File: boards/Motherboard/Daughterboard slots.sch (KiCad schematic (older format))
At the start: 5 parts, among them P701 SLOT-A, P702 SLOT-B, P703 SLOT-C, P704 SLOT-D, P705 SLOT-E

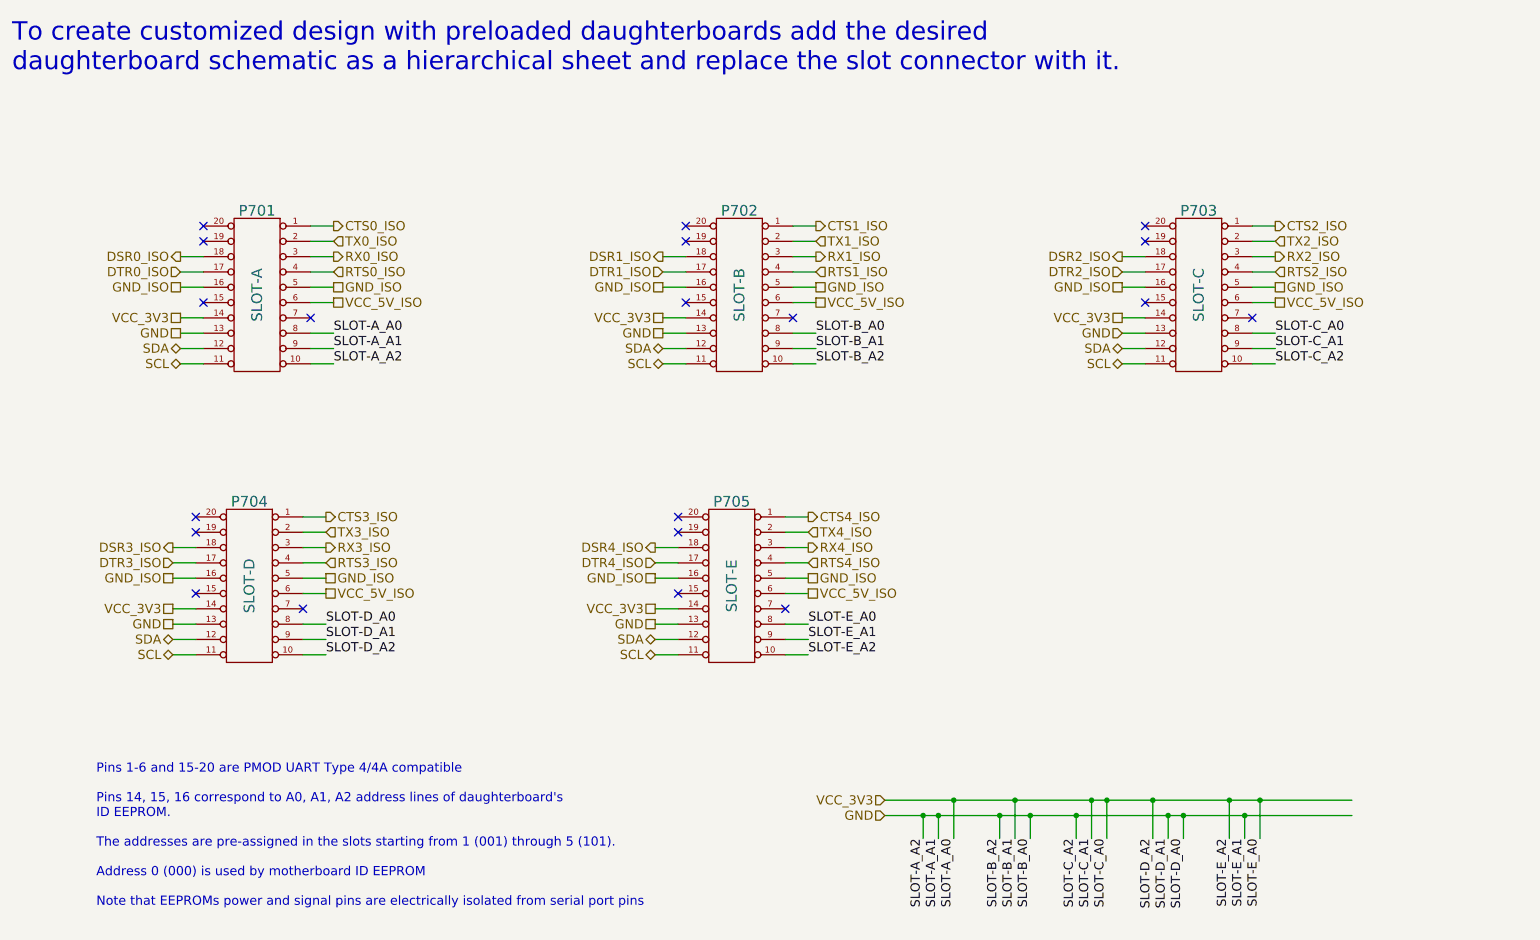
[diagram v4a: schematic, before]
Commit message: Rearranged EEPROM pins in dboard slot pinout to be compatible with PMOD I2C interface
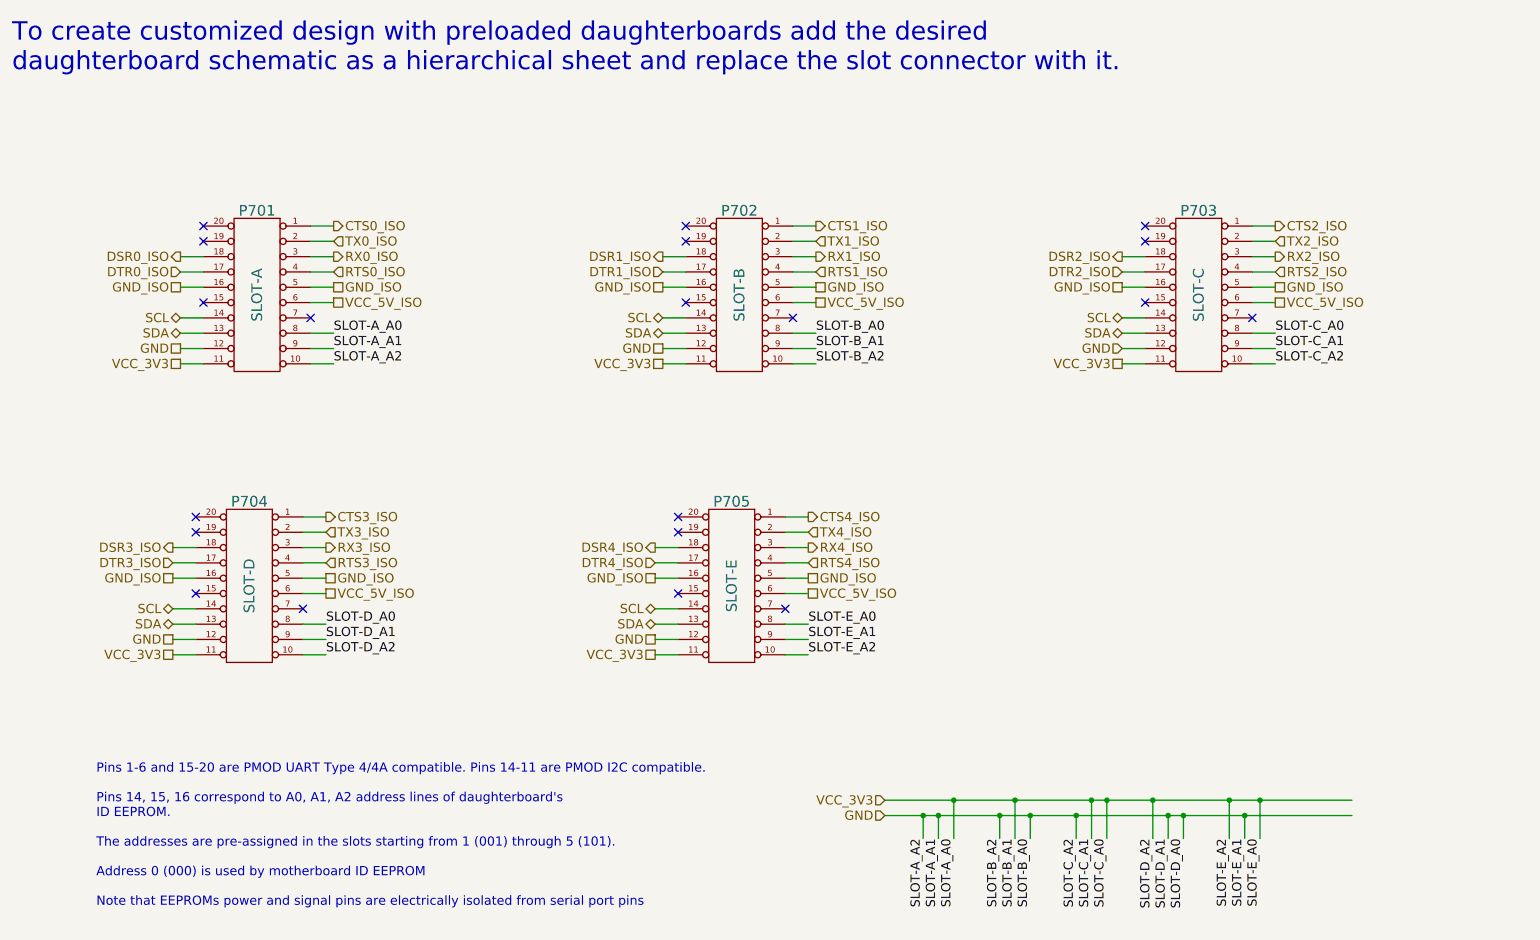
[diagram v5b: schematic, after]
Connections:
- net GND: now also P701.12 (P12), P702.12 (P12), P703.12 (P12), P704.12 (P12), P705.12 (P12); no longer P701.13 (P13), P702.13 (P13), P703.13 (P13), P704.13 (P13), P705.13 (P13)
- net SCL: now also P701.14 (P14), P702.14 (P14), P703.14 (P14), P704.14 (P14), P705.14 (P14); no longer P701.11 (P11), P702.11 (P11), P703.11 (P11), P704.11 (P11), P705.11 (P11)
- net SDA: now also P701.13 (P13), P702.13 (P13), P703.13 (P13), P704.13 (P13), P705.13 (P13); no longer P701.12 (P12), P702.12 (P12), P703.12 (P12), P704.12 (P12), P705.12 (P12)
- net VCC_3V3: now also P701.11 (P11), P702.11 (P11), P703.11 (P11), P704.11 (P11), P705.11 (P11); no longer P701.14 (P14), P702.14 (P14), P703.14 (P14), P704.14 (P14), P705.14 (P14)
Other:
- note added: "Pins 1-6 and 15-20 are PMOD UART Type 4/4A compatible. Pins 14-11 are PMOD I2C compatible.\n\nPins 14, 15, 16 correspond to A0, A1, A2 address lines of daughterboard's \nID EEPROM. \n\nThe addresses are pre-assigned in the slots starting from 1 (001) through 5 (101).\n\nAddress 0 (000) is used by motherboard ID EEPROM\n\nNote that EEPROMs power and signal pins are electrically isolated from seria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"
- note removed: "Pins 1-6 and 15-20 are PMOD UART Type 4/4A compatible\n\nPins 14, 15, 16 correspond to A0, A1, A2 address lines of daughterboard's \nID EEPROM. \n\nThe addresses are pre-assigned in the slots starting from 1 (001) through 5 (101).\n\nAddress 0 (000) is used by motherboard ID EEPROM\n\nNote that EEPROMs power and signal pins are electrically isolated from serial port pins"
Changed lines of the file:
@@
 Sheet 5 7
 Title "Daughterboard interface"
-Date "1 jul 2014"
+Date "2 jul 2014"
 Rev ""
 Comp "TimVideos"
@@
 Text HLabel 3100 2550 2    60   UnSpc ~ 0
 GND_ISO
-Text HLabel 2100 2950 0    60   BiDi ~ 0
+Text HLabel 2100 2850 0    60   BiDi ~ 0
 SDA
 Text Notes 1000 1150 0    120  ~ 0
 To create customized design with preloaded daughterboards add the desired \ndaughterboard schematic as a hierarchical sheet and replace the slot connector with it.
-Text HLabel 2100 3050 0    60   BiDi ~ 0
+Text HLabel 2100 2750 0    60   BiDi ~ 0
 SCL
-Text HLabel 2100 2750 0    60   UnSpc ~ 0
-VCC_3V3
-Text HLabel 2100 2850 0    60   UnSpc ~ 0
+Text HLabel 2100 3050 0    60   UnSpc ~ 0
+VCC_3V3
+Text HLabel 2100 2950 0    60   UnSpc ~ 0
 GND
 Text Notes 1550 6600 0    60   ~ 0
-Pins 1-6 and 15-20 are PMOD UART Type 4/4A compatible\n\nPins 14, 15, 16 correspond to A0, A1, A2 address lines of daughterboard's \nID EEPROM. \n\nThe addresses are pre-assigned in the slots starting from 1 (001) through 5 (101).\n\nAddress 0 (000) is used by motherboard ID EEPROM\n\nNote that EEPROMs power and signal pins are electrically isolated from serial port pins
+Pins 1-6 and 15-20 are PMOD UART Type 4/4A compatible. Pins 14-11 are PMOD I2C compatible.\n\nPins 14, 15, 16 correspond to A0, A1, A2 address lines of daughterboard's \nID EEPROM. \n\nThe addresses are pre-assigned in the slots starting from 1 (001) through 5 (101).\n\nAddress 0 (000) is used by motherboard ID EEPROM\n\nNote that EEPROMs power and signal pins are electrically isolated from serial port pins
 Text Label 3100 2850 0    60   ~ 0
 SLOT-A_A0
@@
 GND
 NoConn ~ 2250 2650
-Text HLabel 5250 2950 0    60   BiDi ~ 0
+Text HLabel 5250 2850 0    60   BiDi ~ 0
 SDA
-Text HLabel 5250 3050 0    60   BiDi ~ 0
+Text HLabel 5250 2750 0    60   BiDi ~ 0
 SCL
-Text HLabel 5250 2850 0    60   UnSpc ~ 0
+Text HLabel 5250 2950 0    60   UnSpc ~ 0
 GND
 Text Label 6250 2850 0    60   ~ 0
@@
 Text Label 6250 3050 0    60   ~ 0
 SLOT-B_A2
-Text HLabel 8250 2950 0    60   BiDi ~ 0
+Text HLabel 8250 2850 0    60   BiDi ~ 0
 SDA
-Text HLabel 8250 3050 0    60   BiDi ~ 0
+Text HLabel 8250 2750 0    60   BiDi ~ 0
 SCL
-Text HLabel 8250 2850 0    60   Input ~ 0
+Text HLabel 8250 2950 0    60   Input ~ 0
 GND
 Text Label 9250 2850 0    60   ~ 0
@@
 	-1   0    0    -1
 $EndComp
-Text HLabel 2050 4850 0    60   BiDi ~ 0
+Text HLabel 2050 4750 0    60   BiDi ~ 0
 SDA
-Text HLabel 2050 4950 0    60   BiDi ~ 0
+Text HLabel 2050 4650 0    60   BiDi ~ 0
 SCL
-Text HLabel 2050 4750 0    60   UnSpc ~ 0
+Text HLabel 2050 4850 0    60   UnSpc ~ 0
 GND
 Text Label 3050 4750 0    60   ~ 0
@@
 	-1   0    0    -1
 $EndComp
-Text HLabel 5200 4850 0    60   BiDi ~ 0
+Text HLabel 5200 4750 0    60   BiDi ~ 0
 SDA
-Text HLabel 5200 4950 0    60   BiDi ~ 0
+Text HLabel 5200 4650 0    60   BiDi ~ 0
 SCL
-Text HLabel 5200 4750 0    60   UnSpc ~ 0
+Text HLabel 5200 4850 0    60   UnSpc ~ 0
 GND
 Text Label 6200 4750 0    60   ~ 0
@@
 	3100 2550 2950 2550
 Wire Wire Line
+	2100 2850 2250 2850
+Wire Wire Line
+	2100 2750 2250 2750
+Wire Wire Line
 	2100 2950 2250 2950
 Wire Wire Line
 	2100 3050 2250 3050
 Wire Wire Line
-	2100 2850 2250 2850
-Wire Wire Line
-	2100 2750 2250 2750
-Wire Wire Line
 	3100 2850 2950 2850
 Wire Wire Line
@@
 	6700 6000 9750 6000
 Wire Wire Line
+	5250 2850 5400 2850
+Wire Wire Line
+	5250 2750 5400 2750
+Wire Wire Line
 	5250 2950 5400 2950
 Wire Wire Line
-	5250 3050 5400 3050
-Wire Wire Line
-	5250 2850 5400 2850
-Wire Wire Line
 	6250 2850 6100 2850
 Wire Wire Line
@@
 	6250 3050 6100 3050
 Wire Wire Line
+	8250 2850 8400 2850
+Wire Wire Line
+	8250 2750 8400 2750
+Wire Wire Line
 	8250 2950 8400 2950
 Wire Wire Line
-	8250 3050 8400 3050
-Wire Wire Line
-	8250 2850 8400 2850
-Wire Wire Line
 	9250 2850 9100 2850
 Wire Wire Line
@@
 	9250 3050 9100 3050
 Wire Wire Line
+	2050 4750 2200 4750
+Wire Wire Line
+	2050 4650 2200 4650
+Wire Wire Line
 	2050 4850 2200 4850
 Wire Wire Line
-	2050 4950 2200 4950
-Wire Wire Line
-	2050 4750 2200 4750
-Wire Wire Line
 	3050 4750 2900 4750
 Wire Wire Line
@@
 	3050 4950 2900 4950
 Wire Wire Line
+	5200 4750 5350 4750
+Wire Wire Line
+	5200 4650 5350 4650
+Wire Wire Line
 	5200 4850 5350 4850
-Wire Wire Line
-	5200 4950 5350 4950
-Wire Wire Line
-	5200 4750 5350 4750
 Wire Wire Line
 	6200 4750 6050 4750
@@
 Wire Wire Line
 	6100 2450 6250 2450
-Text HLabel 5250 2750 0    60   UnSpc ~ 0
-VCC_3V3
-Wire Wire Line
-	5250 2750 5400 2750
+Text HLabel 5250 3050 0    60   UnSpc ~ 0
+VCC_3V3
+Wire Wire Line
+	5250 3050 5400 3050
 NoConn ~ 6100 2750
 Text HLabel 9250 2150 2    60   Output ~ 0
@@
 Wire Wire Line
 	8250 2550 8400 2550
-Text HLabel 8250 2750 0    60   UnSpc ~ 0
-VCC_3V3
-Wire Wire Line
-	8250 2750 8400 2750
+Text HLabel 8250 3050 0    60   UnSpc ~ 0
+VCC_3V3
+Wire Wire Line
+	8250 3050 8400 3050
 NoConn ~ 8400 2650
 NoConn ~ 8400 2250
@@
 NoConn ~ 2200 4550
 NoConn ~ 2900 4650
-Text HLabel 2050 4650 0    60   UnSpc ~ 0
-VCC_3V3
-Wire Wire Line
-	2050 4650 2200 4650
+Text HLabel 2050 4950 0    60   UnSpc ~ 0
+VCC_3V3
+Wire Wire Line
+	2050 4950 2200 4950
 NoConn ~ 6050 4650
 NoConn ~ 5350 4550
@@
 Wire Wire Line
 	5200 4450 5350 4450
-Text HLabel 5200 4650 0    60   UnSpc ~ 0
-VCC_3V3
-Wire Wire Line
-	5200 4650 5350 4650
+Text HLabel 5200 4950 0    60   UnSpc ~ 0
+VCC_3V3
+Wire Wire Line
+	5200 4950 5350 4950
 $EndSCHEMATC

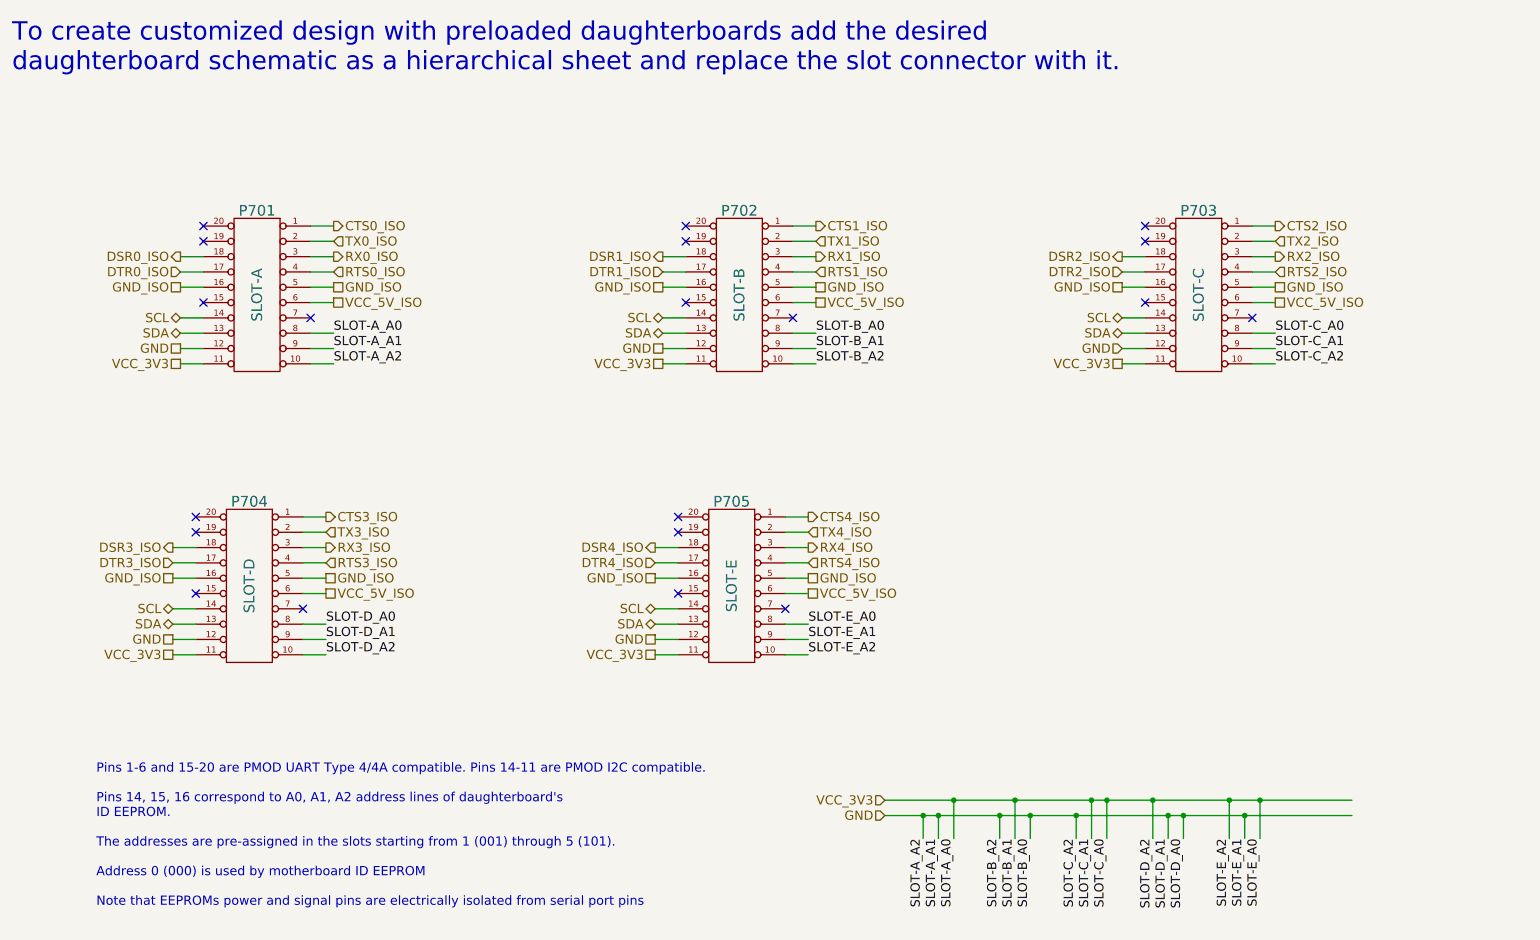
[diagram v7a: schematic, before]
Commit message: Updated motherboard schematic to use new dboard_slot component
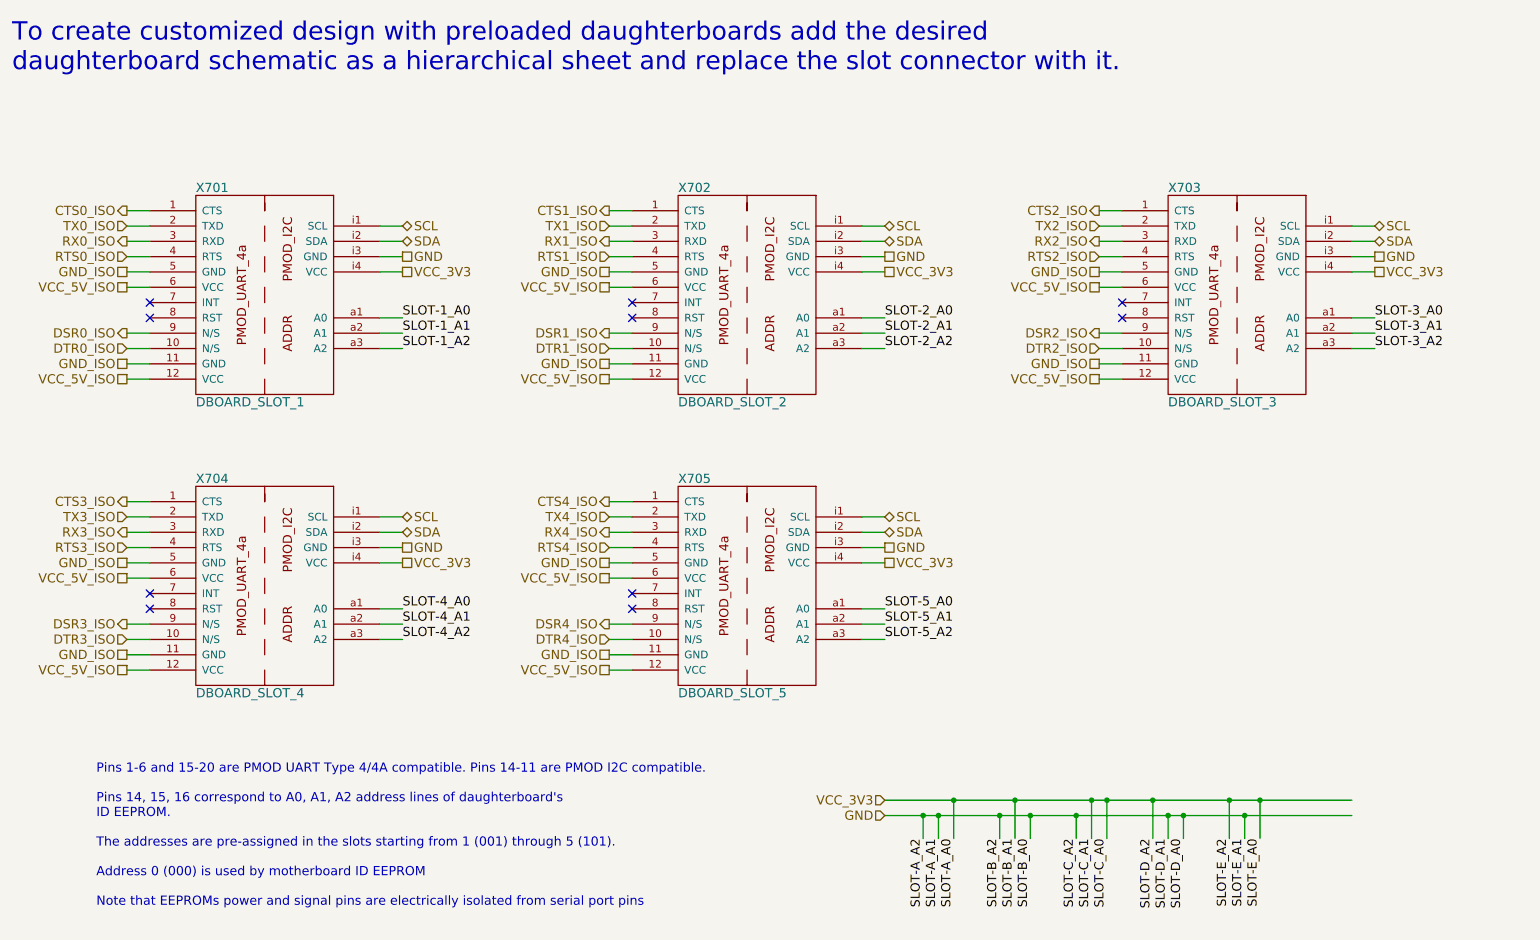
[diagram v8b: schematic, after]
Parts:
- removed P701: SLOT-A, symbol DIL20
- removed P702: SLOT-B, symbol DIL20
- removed P703: SLOT-C, symbol DIL20
- removed P704: SLOT-D, symbol DIL20
- removed P705: SLOT-E, symbol DIL20
- added X701: DBOARD_SLOT_1, ~, symbol DBOARD_SLOT
- added X702: DBOARD_SLOT_2, ~, symbol DBOARD_SLOT
- added X703: DBOARD_SLOT_3, ~, symbol DBOARD_SLOT
- added X704: DBOARD_SLOT_4, ~, symbol DBOARD_SLOT
- added X705: DBOARD_SLOT_5, ~, symbol DBOARD_SLOT
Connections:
- net CTS0_ISO: now also X701.1 (CTS)
- net CTS1_ISO: now also X702.1 (CTS)
- net CTS2_ISO: now also X703.1 (CTS)
- net CTS3_ISO: now also X704.1 (CTS)
- net CTS4_ISO: now also X705.1 (CTS)
- net DSR0_ISO: now also X701.9 (N/S)
- net DSR1_ISO: now also X702.9 (N/S)
- net DSR2_ISO: now also X703.9 (N/S)
- net DSR3_ISO: now also X704.9 (N/S)
- net DSR4_ISO: now also X705.9 (N/S)
- net DTR0_ISO: now also X701.10 (N/S)
- net DTR1_ISO: now also X702.10 (N/S)
- net DTR2_ISO: now also X703.10 (N/S)
- net DTR3_ISO: now also X704.10 (N/S)
- net DTR4_ISO: now also X705.10 (N/S)
- net GND: now also X701.i3 (GND), X702.i3 (GND), X703.i3 (GND), X704.i3 (GND), X705.i3 (GND)
- net GND_ISO: now also X701.11 (GND), X701.5 (GND), X702.11 (GND), X702.5 (GND), X703.11 (GND), X703.5 (GND), X704.11 (GND), X704.5 (GND), X705.11 (GND), X705.5 (GND)
- net RTS0_ISO: now also X701.4 (RTS)
- net RTS1_ISO: now also X702.4 (RTS)
- net RTS2_ISO: now also X703.4 (RTS)
- net RTS3_ISO: now also X704.4 (RTS)
- net RTS4_ISO: now also X705.4 (RTS)
- net RX0_ISO: now also X701.3 (RXD)
- net RX1_ISO: now also X702.3 (RXD)
- net RX2_ISO: now also X703.3 (RXD)
- net RX3_ISO: now also X704.3 (RXD)
- net RX4_ISO: now also X705.3 (RXD)
- net SCL: now also X701.i1 (SCL), X702.i1 (SCL), X703.i1 (SCL), X704.i1 (SCL), X705.i1 (SCL)
- net SDA: now also X701.i2 (SDA), X702.i2 (SDA), X703.i2 (SDA), X704.i2 (SDA), X705.i2 (SDA)
- net TX0_ISO: now also X701.2 (TXD)
- net TX1_ISO: now also X702.2 (TXD)
- net TX2_ISO: now also X703.2 (TXD)
- net TX3_ISO: now also X704.2 (TXD)
- net TX4_ISO: now also X705.2 (TXD)
- net VCC_3V3: now also X701.i4 (VCC), X702.i4 (VCC), X703.i4 (VCC), X704.i4 (VCC), X705.i4 (VCC)
- net VCC_5V_ISO: now also X701.12 (VCC), X701.6 (VCC), X702.12 (VCC), X702.6 (VCC), X703.12 (VCC), X703.6 (VCC), X704.12 (VCC), X704.6 (VCC), X705.12 (VCC), X705.6 (VCC)
- new net SLOT-1_A0: X701.a1 (A0)
- new net SLOT-1_A1: X701.a2 (A1)
- new net SLOT-1_A2: X701.a3 (A2)
- new net SLOT-2_A0: X702.a1 (A0)
- new net SLOT-2_A1: X702.a2 (A1)
- new net SLOT-2_A2: X702.a3 (A2)
- new net SLOT-3_A0: X703.a1 (A0)
- new net SLOT-3_A1: X703.a2 (A1)
- new net SLOT-3_A2: X703.a3 (A2)
- new net SLOT-4_A0: X704.a1 (A0)
- new net SLOT-4_A1: X704.a2 (A1)
- new net SLOT-4_A2: X704.a3 (A2)
- new net SLOT-5_A0: X705.a1 (A0)
- new net SLOT-5_A1: X705.a2 (A1)
- new net SLOT-5_A2: X705.a3 (A2)
- no-connect marks 20 -> 10
